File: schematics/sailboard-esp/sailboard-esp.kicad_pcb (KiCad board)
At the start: 2 copper layers, 105.4 x 51.4 mm, 31 parts, among them U3 L293D

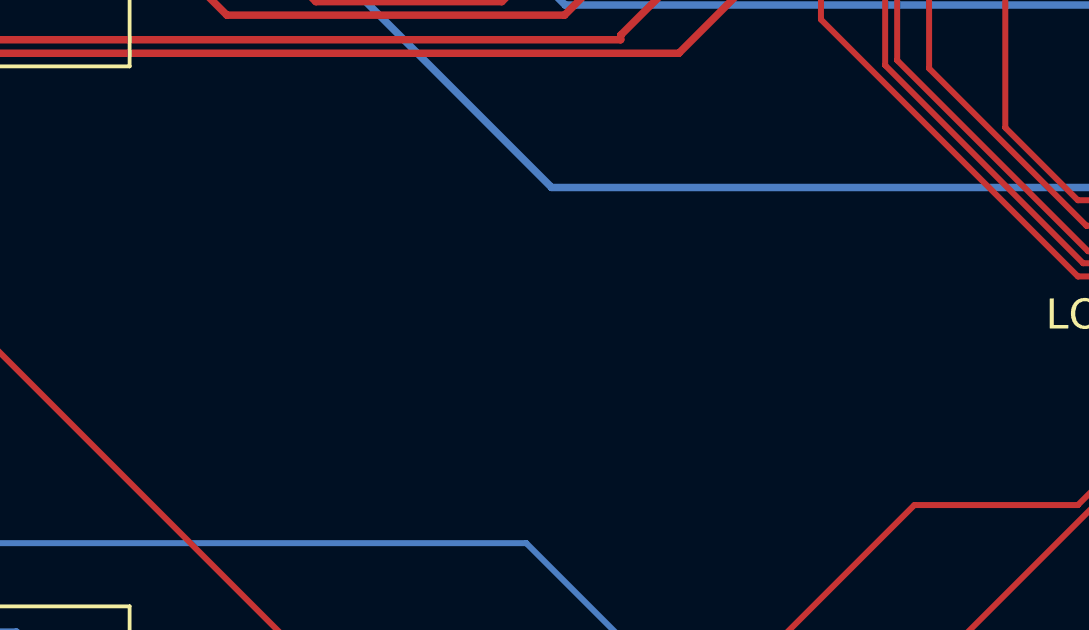
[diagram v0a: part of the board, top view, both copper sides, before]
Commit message: add version to silkscreen.
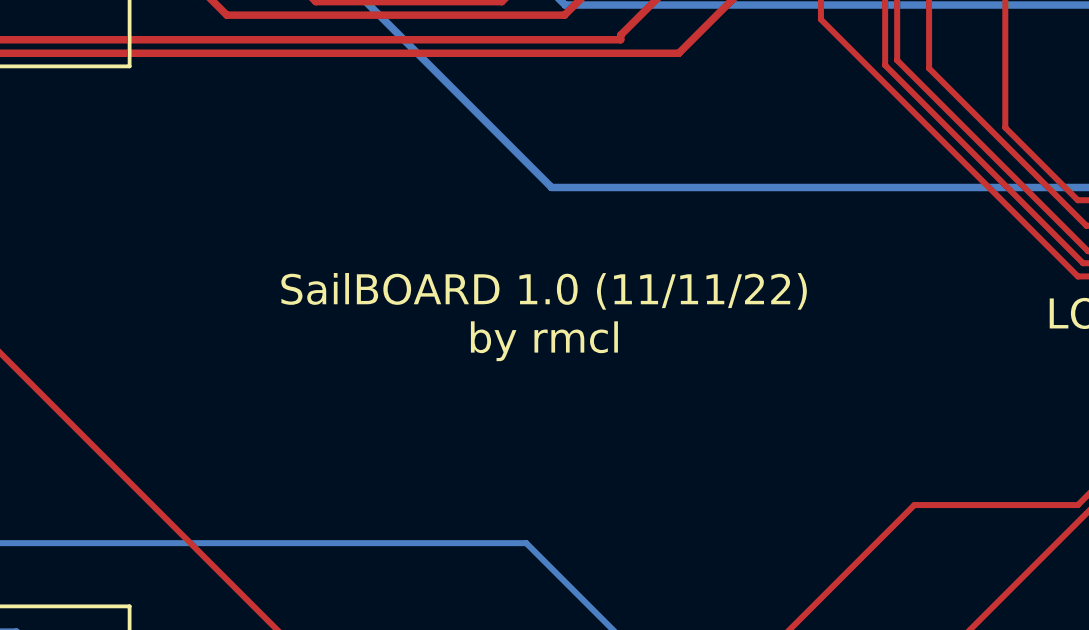
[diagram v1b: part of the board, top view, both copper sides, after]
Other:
- board text added: "SailBOARD 1.0 (11/11/22) by rmcl"
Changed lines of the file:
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@@
   (gr_rect (start 203.2 22.86) (end 184.15 38.1) (layer "F.SilkS") (width 0.2) (fill none))
   (gr_rect (start 149.86 22.55) (end 255.27 73.93) (layer "Edge.Cuts") (width 0.2) (fill none))
+  (gr_text "SailBOARD 1.0 (11/11/22)\nby rmcl " (at 191.77 52.34) (layer "F.SilkS")
+    (effects (font (size 1 1) (thickness 0.15)))
+  )
   (segment (start 224.79 47.26) (end 222.25 44.72) (width 0.2) (layer "F.Cu") (net 1))
   (segment (start 234.475 71.19) (end 243.66 71.19) (width 0.25) (layer "F.Cu") (net 1))

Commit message: v1.1 of sailboard.
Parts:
- removed C1, C3: C, Capacitor_SMD:C_0603_1608Metric
- removed C2: .1uF, Capacitor_SMD:C_0603_1608Metric
- removed C4: 10uF, Capacitor_SMD:C_0603_1608Metric
- removed LOGICTRANS1: TXB0108DQSR, Package_SON:USON-20_2x4mm_P0.4mm
- removed SDCARD1: SD Card, Connector_PinHeader_2.00mm:PinHeader_1x06_P2.00mm_Vertical
- added BATCHRG1: BatteryCharge, Connector_PinHeader_2.00mm:PinHeader_1x02_P2.00mm_Vertical, F.Cu at (251.5, 71.4)
- added CURRENT_SOLAR1: INA219BxD, Package_SO:SOIC-8_3.9x4.9mm_P1.27mm, F.Cu at (232.4, 68.8)
- added H1: MountingHole_2.2mm_M2, MountingHole:MountingHole_2.2mm_M2, F.Cu at (161.3, 29.5)
- added LEVEL_TRANSLATE1: TXB0108PWR, SOP65P640X120-20N:SOP65P640X120-20N, F.Cu at (205.7, 57.4)
- added MICRO_SD1: Micro_SD_Card, Connector_Card:microSD_HC_Molex_104031-0811, F.Cu at (166.4, 63.8)
- added REF**: MountingHole_2.2mm_M2, MountingHole:MountingHole_2.2mm_M2, F.Cu at (240.0, 37.1)
- added REF**: MountingHole_2.2mm_M2, MountingHole:MountingHole_2.2mm_M2, F.Cu at (152.9, 70.9)
- added REF**: MountingHole_2.2mm_M2, MountingHole:MountingHole_2.2mm_M2, F.Cu at (245.3, 60.6)
- added R_SHUNT2: 100mOhms, Resistor_SMD:R_2512_6332Metric, F.Cu at (242.6, 68.8)
- added SOLARIN1: SolarPanel, Connector_PinHeader_2.00mm:PinHeader_1x02_P2.00mm_Vertical, F.Cu at (251.5, 63.8)
- BATIN1, MOTOR1, MOTOR2: footprint Connector_PinHeader_2.54mm:PinHeader_1x02_P2.54mm_Vertical -> Connector_PinHeader_2.00mm:PinHeader_1x02_P2.00mm_Vertical
- COMPASS1: footprint Connector_PinHeader_2.00mm:PinHeader_1x05_P2.00mm_Vertical -> Connector_PinHeader_2.54mm:PinHeader_1x05_P2.54mm_Vertical
- ESP32: footprint ESP32-DEVKITC:MODULE_ESP32-DEVKITC -> ESP32-DEVKITC:MODULE_ESP32-DEVKITC-RESIZED
- MAINSWITCH1: renamed from POWER SWITCH; footprint Connector_PinHeader_2.54mm:PinHeader_1x02_P2.54mm_Vertical -> Connector_PinHeader_2.00mm:PinHeader_1x02_P2.00mm_Vertical
- RUDDER1: footprint Connector_PinHeader_2.54mm:PinHeader_1x03_P2.54mm_Vertical -> Connector_PinHeader_2.00mm:PinHeader_1x03_P2.00mm_Vertical
- moved ESP32 26.6 mm to (176.3, 59.5)
- moved Regulator5V 25.3 mm to (237.5, 43.5), turned to 90 degrees
- moved R2 21.1 mm to (224.8, 43.5), turned to -90 degrees
- moved R3 21.0 mm to (234.9, 48.5)
- moved R4 17.3 mm to (237.5, 47.3), turned to 90 degrees
- moved R5 16.6 mm to (240.0, 47.3), turned to -90 degrees
- moved Regulator3V 15.0 mm to (229.9, 43.5), turned to 90 degrees
- moved R_SHUNT1 14.7 mm to (243.8, 52.8), turned to -90 degrees
- moved CURRENT_MAIN1 13.1 mm to (234.9, 54.9), turned to 0 degrees
- moved D2 12.5 mm to (241.3, 61.2)
- moved R1 11.3 mm to (237.5, 62.5), turned to 90 degrees
- moved R7 7.51 mm to (229.9, 49.8), turned to 0 degrees
- moved RADIO1 6.84 mm to (163.8, 51.1)
- moved R6 5.92 mm to (229.9, 47.3), turned to 180 degrees
- moved BATIN1 5.08 mm to (251.5, 57.4)
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- renumbered CURRENT_SENSOR1 to CURRENT_MAIN1, Regulator3V1 to Regulator3V, Regulator5V1 to Regulator5V
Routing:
- net +5V: track 275.4 -> 247.1 mm
- net /RADIO_CHAN1_5V: track 87.3 -> 62.1 mm
- net /RADIO_CHAN2_5V: track 81.0 -> 56.9 mm
- net /Microcontroller/PROP_ENABLE_2_5V: track 39.6 -> 61.5 mm
- net /Power/Battery Charge Pos: track 0.00 -> 18.2 mm
- net /Power/Solar Pos: track 0.00 -> 17.9 mm
- net Net-(ESP32-Pad25): track 26.9 -> 13.9 mm
- net /Microcontroller/PROP_PWM_5V: track 24.6 -> 36.2 mm
- net +12V: track 80.1 -> 69.5 mm, vias 0 -> 1
- net /SCK: track 88.0 -> 97.8 mm
- net Net-(ESP32-Pad26): track 21.7 -> 12.2 mm
- net /MISO: track 90.1 -> 98.9 mm, vias 0 -> 1
- net +3.3V: track 185.3 -> 193.6 mm, vias 2 -> 1
- net /SDA: track 135.6 -> 143.7 mm
- net /Microcontroller/PROP_ENABLE_1_5V: track 28.1 -> 35.8 mm
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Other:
- board text added: "SailBOARD 1.1 (11/22/22) by rmcl"
- board text removed: "SailBOARD 1.0 (11/11/22) by rmcl"

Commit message: version 1.1.
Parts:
- BATCHRG1, BATIN1, MAINSWITCH1, MOTOR1, MOTOR2, SOLARIN1: footprint Connector_PinHeader_2.00mm:PinHeader_1x02_P2.00mm_Vertical -> Connector_PinHeader_2.54mm:PinHeader_1x02_P2.54mm_Vertical
- LED: renamed from D2; footprint LED_SMD:LED_0402_1005Metric -> LED_SMD:LED_0603_1608Metric
- RUDDER1: footprint Connector_PinHeader_2.00mm:PinHeader_1x03_P2.00mm_Vertical -> Connector_PinHeader_2.54mm:PinHeader_1x03_P2.54mm_Vertical
- moved SOLARIN1 2.84 mm to (248.9, 65.0), turned to 90 degrees
- moved BATCHRG1 2.74 mm to (248.9, 70.4), turned to 90 degrees
- moved R1 1.27 mm to (237.5, 61.2), turned to 0 degrees
- moved D1 0.89 mm to (246.8, 46.7)
- moved MOTOR2 0.55 mm to (251.5, 31.0)
- moved LED 0.43 mm to (240.9, 61.2)
- moved RUDDER1 0.31 mm to (251.5, 37.4)
- moved MOTOR1 0.26 mm to (251.3, 24.8)
- renumbered Regulator3V to Regulator3V1, Regulator5V to Regulator5V1
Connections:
- CURRENT_MAIN1 pad 5: +5V -> +3.3V
- CURRENT_SOLAR1 pad 2: +5V -> +3.3V
- CURRENT_SOLAR1 pad 5: +5V -> +3.3V
- R1 pad 1: +5V -> +3.3V
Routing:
- net +3.3V: track 193.6 -> 247.2 mm, vias 1 -> 2
- net +5V: track 247.1 -> 207.5 mm
- net Net-(MOTOR2-Pad2): track 23.8 -> 28.6 mm
- net GND: track 403.4 -> 398.8 mm
- net /Power/Solar Pos: track 17.9 -> 14.8 mm
- net /Power/Battery Charge Pos: track 18.2 -> 16.1 mm
- net /Power/Battery Charge Neg: track 3.62 -> 5.42 mm
- net Net-(D2-Pad2): track 3.51 -> 1.76 mm
- net Net-(BATIN1-Pad2): track 10.5 -> 11.7 mm
- net Net-(MOTOR1-Pad2): track 16.0 -> 14.9 mm
- net /SDA: track 143.7 -> 144.7 mm
- net /Power/Battery Input: track 13.5 -> 12.6 mm
- net Net-(MOTOR1-Pad1): track 24.4 -> 23.6 mm
- net Net-(MOTOR2-Pad1): track 15.7 -> 15.1 mm
- net Net-(CURRENT_MAIN1-Pad8): track 12.6 -> 12.0 mm
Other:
- board text added: "SailBOARD 1.1 (11/26/22) by rmcl"
- board text removed: "SailBOARD 1.1 (11/22/22) by rmcl"

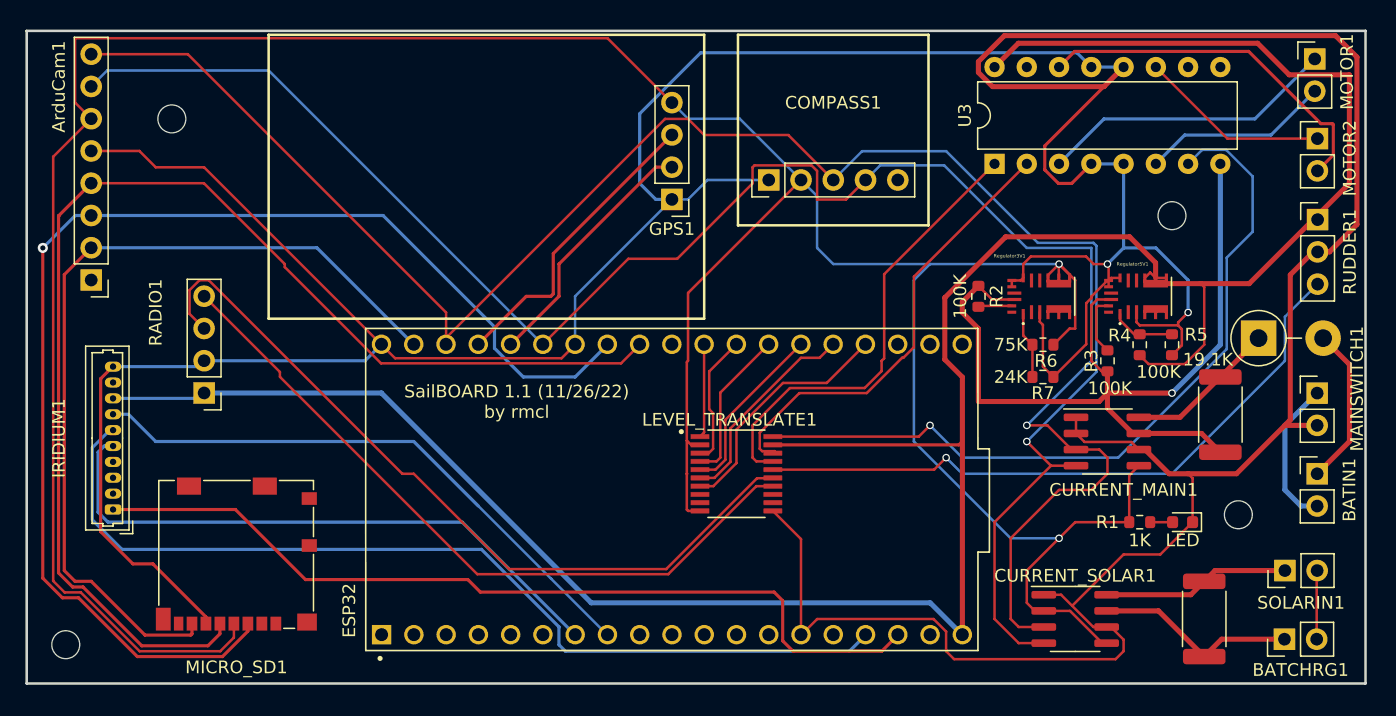
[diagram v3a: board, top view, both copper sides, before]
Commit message: add capacitor footprint.
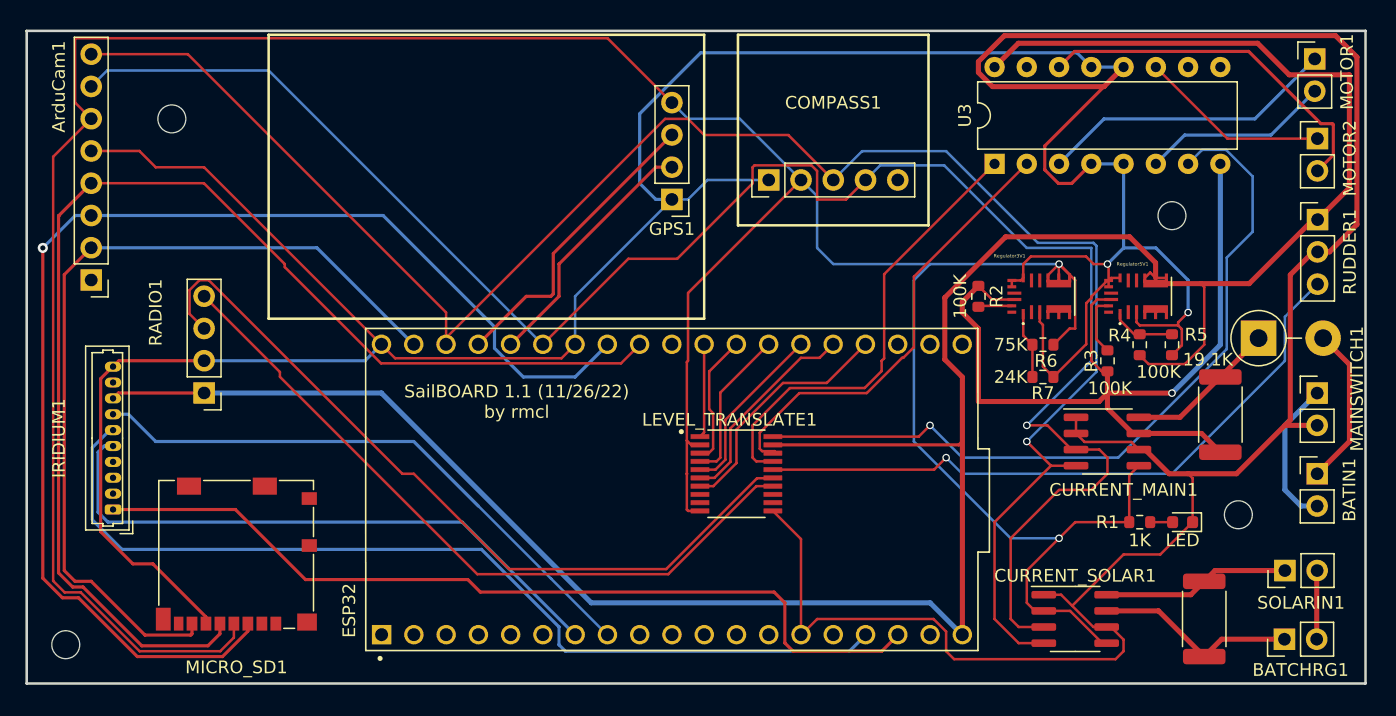
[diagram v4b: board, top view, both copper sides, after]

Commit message: move to version 1.2.
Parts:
- removed LEVEL_TRANSLATE1: TXB0108PWR, SOP65P640X120-20N:SOP65P640X120-20N
- removed MOTOR2: MOTOR, Connector_PinHeader_2.54mm:PinHeader_1x02_P2.54mm_Vertical
- removed R6: 75K, Resistor_SMD:R_0603_1608Metric
- removed R7: 24K, Resistor_SMD:R_0603_1608Metric
- removed Regulator3V1: MPM3610AGQV-P, MPM3610AGQV-P:MPM3620AGQV-P
- removed U3: L293D, Package_DIP:DIP-16_W7.62mm
- added C1: 1u, Capacitor_SMD:C_0603_1608Metric_Pad1.08x0.95mm_HandSolder, F.Cu at (208.3, 40.9)
- added C2: 10uF, Capacitor_SMD:C_0603_1608Metric_Pad1.08x0.95mm_HandSolder, F.Cu at (170.2, 30.7)
- added C3: 22uF, Capacitor_SMD:C_0603_1608Metric_Pad1.08x0.95mm_HandSolder, F.Cu at (182.4, 29.6)
- added IC1: TXB0108PWR, SOP65P640X120-20N:SOP65P640X120-20N, F.Cu at (198.1, 57.4)
- added U1: AP2112K-3.3, Package_TO_SOT_SMD:SOT-23-5, F.Cu at (213.4, 40.9)
- added U2: L293D, Package_DIP:DIP-16_W7.62mm, F.Cu at (223.5, 25.7)
- BATCHRG1, BATIN1, MAINSWITCH1, MOTOR1, SOLARIN1: footprint Connector_PinHeader_2.54mm:PinHeader_1x02_P2.54mm_Vertical -> Connector_JST:JST_XH_B2B-XH-A_1x02_P2.50mm_Vertical
- H1, REF** (x3): value MountingHole_2.2mm_M2 -> MountingHole_2.5mm; footprint MountingHole:MountingHole_2.2mm_M2 -> MountingHole:MountingHole_2.5mm
- R2: value 100K -> 39K
- R5: value 19.1K -> 19K
- RUDDER1: footprint Connector_PinHeader_2.54mm:PinHeader_1x03_P2.54mm_Vertical -> Connector_JST:JST_XH_B3B-XH-A_1x03_P2.50mm_Vertical
- moved R3 64.8 mm to (171.5, 35.4), turned to -90 degrees
- moved Regulator5V1 62.4 mm to (176.4, 30.4)
- moved R4 60.9 mm to (177.8, 35.4)
- moved R5 60.9 mm to (180.3, 35.4)
- moved R_SHUNT1 60.5 mm to (188.6, 28.1), turned to 180 degrees
- moved R2 50.5 mm to (175.0, 34.5), turned to 0 degrees
- moved CURRENT_MAIN1 50.5 mm to (188.8, 34.5)
- moved BATIN1 31.2 mm to (236.2, 30.2)
- moved R_SHUNT2 26.2 mm to (218.4, 58.7)
- moved CURRENT_SOLAR1 25.0 mm to (209.6, 58.7)
- moved MOTOR1 25.0 mm to (236.4, 44.8)
- moved D1 24.5 mm to (235.3, 25.1)
- moved RUDDER1 23.2 mm to (234.9, 53.6)
- moved MAINSWITCH1 20.6 mm to (236.3, 37.2)
- moved REF** 19.1 mm to (228.7, 70.0)
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- renumbered LED to D2
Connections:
- ArduCam1 pad 1: /CS -> /ARDUCAM_CS
- ESP32 pad 10: unconnected-(ESP32-Pad10) -> /ARDUCAM_CS
- ESP32 pad 12: unconnected-(ESP32-Pad12) -> /SDCARD_SCK
- ESP32 pad 13: unconnected-(ESP32-Pad13) -> /SDCARD_D2
- ESP32 pad 15: unconnected-(ESP32-Pad15) -> /SDCARD_D3
- ESP32 pad 23: Net-(ESP32-Pad23) -> /SDCARD_CMD
- ESP32 pad 24: Net-(ESP32-Pad24) -> /SDCARD_D0
- ESP32 pad 26: Net-(ESP32-Pad26) -> /SDCARD_D1
- ESP32 pad 5: unconnected-(ESP32-Pad5) -> /Microcontroller/RUDDER_PWM
- ESP32 pad 6: unconnected-(ESP32-Pad6) -> /IRIDIUM_SLEEP
- ESP32 pad 8: /IRIDIUM_SLEEP -> /Microcontroller/RADIO_CHAN1
- ESP32 pad 9: unconnected-(ESP32-Pad9) -> /Microcontroller/RADIO_CHAN2
- MICRO_SD1 pad 1: unconnected-(MICRO_SD1-Pad1) -> /SDCARD_D2
- MICRO_SD1 pad 2: /SDCARD_CS -> /SDCARD_D3
- MICRO_SD1 pad 3: /MISO -> /SDCARD_CMD
- MICRO_SD1 pad 5: /SCK -> /SDCARD_SCK
- MICRO_SD1 pad 7: /MOSI -> /SDCARD_D0
- MICRO_SD1 pad 8: unconnected-(MICRO_SD1-Pad8) -> /SDCARD_D1
- R2 pad 1: +12V -> Net-(R2-Pad1)
- R2 pad 2: Net-(R2-Pad2) -> GND
- Regulator5V1 pad 18: unconnected-(Regulator5V1-Pad18) -> Net-(R2-Pad1)
- Regulator5V1 pad 19: Net-(Regulator5V1-Pad19) -> unconnected-(Regulator5V1-Pad19)
- Regulator5V1 pad 4: Net-(Regulator5V1-Pad19) -> unconnected-(Regulator5V1-Pad19)
- Regulator5V1 pad 5: Net-(Regulator5V1-Pad19) -> unconnected-(Regulator5V1-Pad19)
- Regulator5V1 pad 6: Net-(Regulator5V1-Pad19) -> unconnected-(Regulator5V1-Pad19)
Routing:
- net /ARDUCAM_CS: track 0.00 -> 66.2 mm, vias 0 -> 1
- net /SDCARD_D0: track 0.00 -> 66.1 mm, vias 0 -> 1
- net /SDCARD_CMD: track 0.00 -> 61.9 mm, vias 0 -> 1
- net /SDCARD_D1: track 0.00 -> 61.7 mm, vias 0 -> 1
- net /MISO: track 98.9 -> 43.2 mm, vias 1 -> 0
- net /SCK: track 97.8 -> 46.9 mm
- net /SDCARD_D3: track 0.00 -> 50.9 mm
- net /SDCARD_SCK: track 0.00 -> 44.1 mm, vias 0 -> 1
- net /SDCARD_D2: track 0.00 -> 43.1 mm
- net +12V: track 69.5 -> 110.9 mm, vias 1 -> 0
- net Net-(CURRENT_MAIN1-Pad8): track 12.0 -> 52.5 mm
- net /MOSI: track 67.9 -> 29.4 mm
- net GND: track 398.8 -> 361.8 mm, vias 2 -> 3
- net +5V: track 207.7 -> 238.9 mm, vias 0 -> 2
- net /Microcontroller/PROP_ENABLE_2_5V: track 61.5 -> 32.0 mm, vias 1 -> 0
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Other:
- board size 105.4 x 51.4 mm -> 91.4 x 51.4 mm
- board text added: "SailBOARD 1.2 (12/9/22) by rmcl"
- board text removed: "SailBOARD 1.1 (11/26/22) by rmcl"

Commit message: additional tweaks to version 1.2.
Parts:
- added H1: MountingHole_2.5mm, MountingHole:MountingHole_2.5mm, F.Cu at (170.2, 52.3)
- added H1: MountingHole_2.5mm, MountingHole:MountingHole_2.5mm, F.Cu at (170.5, 43.8)
- added H1: MountingHole_2.5mm, MountingHole:MountingHole_2.5mm, F.Cu at (163.0, 37.1)
- added REF**: MountingHole_2.5mm, MountingHole:MountingHole_2.5mm, F.Cu at (206.6, 43.7)
- added REF**: MountingHole_2.5mm, MountingHole:MountingHole_2.5mm, F.Cu at (213.4, 26.9)
- moved C1 1.80 mm to (209.6, 39.6)
- moved GPS1 1.27 mm to (200.7, 37.1)
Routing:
- net +3.3V: track 264.0 -> 258.9 mm
- net +5V: track 238.9 -> 241.7 mm
- net GND: track 361.8 -> 359.0 mm
- net /SCK: track 46.9 -> 48.3 mm
- net /SCL: track 122.3 -> 120.9 mm
- net /GPS_RX: track 25.7 -> 25.1 mm
- net /GPS_TX: track 22.1 -> 21.6 mm
- net /MISO: track 43.2 -> 43.7 mm
